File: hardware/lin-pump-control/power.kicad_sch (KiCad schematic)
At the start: 22 parts, among them U4 LTC3203BEDD-PBF, U5 BD9G341EFJ

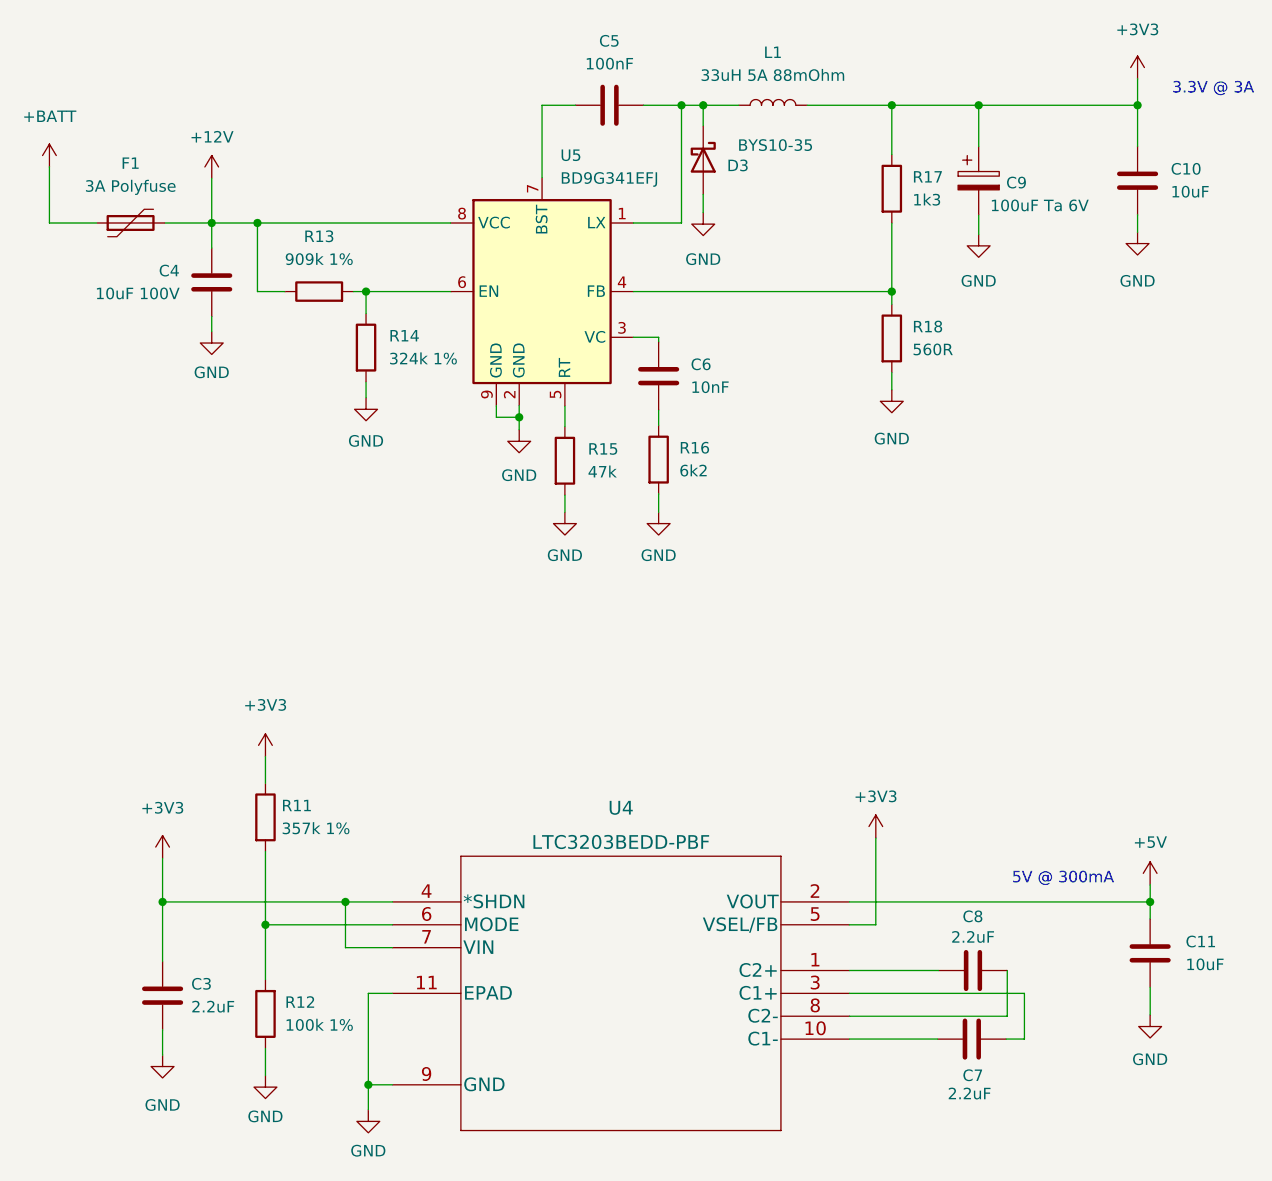
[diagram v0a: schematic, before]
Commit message: Add INA219 to pump controller, change to using regulator module
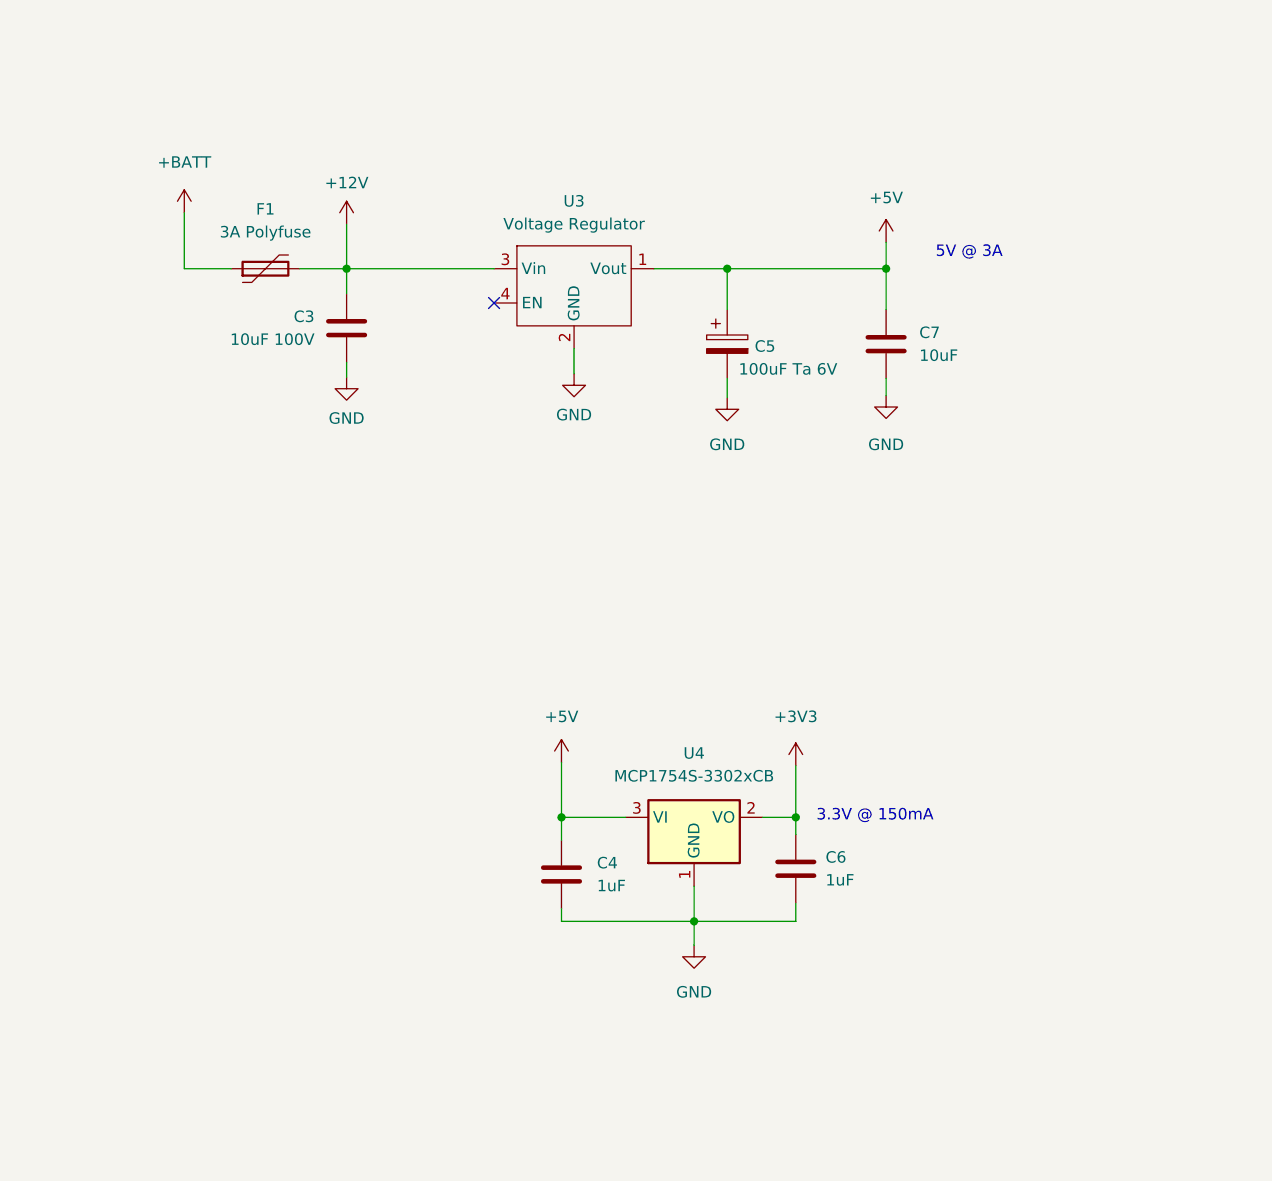
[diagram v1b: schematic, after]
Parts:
- removed C10, C11: 10uF, Capacitor_SMD:C_0805_2012Metric_Pad1.18x1.45mm_HandSolder, symbol Device:C
- removed C5: 100nF, Capacitor_SMD:C_0805_2012Metric_Pad1.18x1.45mm_HandSolder, symbol Device:C
- removed C8: 2.2uF, Capacitor_SMD:C_0805_2012Metric_Pad1.18x1.45mm_HandSolder, symbol Device:C
- removed C9: 100uF Ta 6V, Capacitor_Tantalum_SMD:CP_EIA-3216-10_Kemet-I_Pad1.58x1.35mm_HandSolder, symbol Device:C_Polarized
- removed D3: BYS10-35, Diode_SMD:D_SMA_Handsoldering, symbol Device:D_Schottky
- removed L1: 33uH 5A 88mOhm, Beirdo:PM4346.333NLT, symbol Device:L
- removed R11: 357k 1%, Resistor_SMD:R_0805_2012Metric_Pad1.20x1.40mm_HandSolder, symbol Device:R
- removed R12: 100k 1%, Resistor_SMD:R_0805_2012Metric_Pad1.20x1.40mm_HandSolder, symbol Device:R
- removed R13: 909k 1%, Resistor_SMD:R_0805_2012Metric_Pad1.20x1.40mm_HandSolder, symbol Device:R
- removed R14: 324k 1%, Resistor_SMD:R_0805_2012Metric_Pad1.20x1.40mm_HandSolder, symbol Device:R
- removed R15: 47k, Resistor_SMD:R_0805_2012Metric_Pad1.20x1.40mm_HandSolder, symbol Device:R
- removed R16: 6k2, Resistor_SMD:R_0805_2012Metric_Pad1.20x1.40mm_HandSolder, symbol Device:R
- removed R17: 1k3, Resistor_SMD:R_0805_2012Metric_Pad1.20x1.40mm_HandSolder, symbol Device:R
- removed R18: 560R, Resistor_SMD:R_0805_2012Metric_Pad1.20x1.40mm_HandSolder, symbol Device:R
- removed U4: LTC3203BEDD-PBF, UltraLibrarian:LTC3203BEDD-PBF, symbol UltraLibrarian:LTC3203BEDD-PBF
- removed U5: BD9G341EFJ, Package_SO:HTSOP-8-1EP_3.9x4.9mm_P1.27mm_EP2.4x3.2mm_ThermalVias, symbol Beirdo:BD9G341EFJ
- added C5: 100uF Ta 6V, Capacitor_Tantalum_SMD:CP_EIA-3216-10_Kemet-I_Pad1.58x1.35mm_HandSolder, symbol Device:C_Polarized
- added U3: Voltage Regulator, Beirdo:Switching_Regulator_Module, symbol Beirdo:Switching_Regulator_Module
- added U4: MCP1754S-3302xCB, Package_TO_SOT_SMD:SOT-23, symbol Regulator_Linear:MCP1754S-3302xCB
- C3: value 2.2uF -> 10uF 100V; footprint Capacitor_SMD:C_0805_2012Metric_Pad1.18x1.45mm_HandSolder -> Capacitor_SMD:C_1210_3225Metric_Pad1.33x2.70mm_HandSolder
- C4: value 10uF 100V -> 1uF; footprint Capacitor_SMD:C_1210_3225Metric_Pad1.33x2.70mm_HandSolder -> Capacitor_SMD:C_0805_2012Metric_Pad1.18x1.45mm_HandSolder
- C6: value 10nF -> 1uF
- C7: value 2.2uF -> 10uF
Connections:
- net +12V: now also C3.1, U3.3 (Vin); no longer C4.1
- net +3V3: now also C6.1, U4.2 (VO); no longer C3.1
- net +5V: now also C4.1, C7.1, C5.1, U3.1 (Vout), U4.3 (VI)
- net GND: now also C6.2, C7.2, C5.2, U3.2 (GND), U4.1 (GND)
- no-connect marks 0 -> 1
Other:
- note added: "3.3V @ 150mA"
- note added: "5V @ 3A"
- note removed: "3.3V @ 3A"
- note removed: "5V @ 300mA"
